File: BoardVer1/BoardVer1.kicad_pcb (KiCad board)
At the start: 2 copper layers, 80 parts, among them J1 Vin, J2 Motor conn, J3 FTDI_basic, J4 LED strip, J5 Swiss Sonic cable, J6 CycleStartBtn, J7 MicroSwitches, J8 Estop, J9 SonicGND, SW1 SW_Push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

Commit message: First layout complete
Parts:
- removed C1: 100uF, Capacitor_SMD:C_0805_2012Metric_Pad1.15x1.40mm_HandSolder
- removed C12, C13: 15p, Capacitor_SMD:C_0805_2012Metric_Pad1.15x1.40mm_HandSolder
- removed C8, C9: 100n, Capacitor_SMD:C_0805_2012Metric_Pad1.15x1.40mm_HandSolder
- removed D3: D_Schottky, Diode_SMD:D_SMB_Handsoldering
- removed J3: FTDI_basic, Connector_PinHeader_2.54mm:PinHeader_1x06_P2.54mm_Vertical
- removed L1: 47uH, Inductor_SMD:L_Neosid_SM-NE127_HandSoldering
- removed R2: 1K, Resistor_SMD:R_0805_2012Metric_Pad1.15x1.40mm_HandSolder
- removed R3: 3K, Resistor_SMD:R_0805_2012Metric_Pad1.15x1.40mm_HandSolder
- removed R4: 10K, Resistor_SMD:R_0805_2012Metric_Pad1.15x1.40mm_HandSolder
- removed SW1: SW_Push, Button_Switch_SMD:SW_SPST_B3S-1000
- removed U3: ATMEGA328PB-AU_Arduino, Package_QFP:TQFP-32_7x7mm_P0.8mm
- removed Y1: 16MHZ, Crystal:Crystal_HC49-4H_Vertical
- added A1: Arduino_Nano_v3.x, Module:Arduino_Nano, F.Cu at (174.8, 57.5)
- C15, C17, D1, R10, R11, R13, R17, R19, R22, R5, R6, R8: moved to B.Cu
- C2: value 100uF -> 10uF/50V; footprint Capacitor_SMD:C_0805_2012Metric_Pad1.15x1.40mm_HandSolder -> Capacitor_SMD:C_2010_5025Metric_Pad1.52x2.65mm_HandSolder
- C3: value 10n -> 22uF/16V; footprint Capacitor_SMD:C_0805_2012Metric_Pad1.15x1.40mm_HandSolder -> Capacitor_SMD:C_2010_5025Metric_Pad1.52x2.65mm_HandSolder
- F1: footprint Fuse:Fuse_1210_3225Metric_Pad1.42x2.65mm_HandSolder -> Fuse:Fuse_2010_5025Metric_Pad1.52x2.65mm_HandSolder; moved to B.Cu
- F2: footprint Fuse:Fuse_1210_3225Metric_Pad1.42x2.65mm_HandSolder -> Fuse:Fuse_2010_5025Metric_Pad1.52x2.65mm_HandSolder
- J1: footprint TerminalBlock_4Ucon:TerminalBlock_4Ucon_1x02_P3.50mm_Horizontal -> TerminalBlock:TerminalBlock_bornier-2_P5.08mm
- U2: value LM2675M-ADJ -> V7805-1000; footprint Package_SO:SOIC-8_3.9x4.9mm_P1.27mm -> digikey-footprints:3-SIP_Module_V7805-1000
- moved R11 329.8 mm to (127.2, 55.1)
- moved C14 328.6 mm to (118.1, 63.8), turned to 270 degrees
- moved R1 281.7 mm to (115.6, 70.1), turned to 270 degrees
- moved C10 275.8 mm to (111.0, 66.0), turned to 180 degrees
- moved R19 273.8 mm to (136.4, 129.3), turned to 90 degrees
- moved C15 256.3 mm to (133.9, 85.3)
- moved C17 248.7 mm to (136.9, 76.7), turned to 90 degrees
- moved R18 235.8 mm to (140.5, 124.0), turned to 270 degrees
- moved R21 235.8 mm to (153.2, 123.2)
- moved R22 232.7 mm to (156.2, 106.4)
- moved C2 225.5 mm to (161.5, 105.9), turned to 90 degrees
- moved C3 221.0 mm to (167.1, 106.2), turned to 90 degrees
- moved R10 220.2 mm to (160.0, 47.8), turned to 270 degrees
- moved R5 212.5 mm to (185.2, 62.5), turned to 180 degrees
- moved R9 208.7 mm to (170.9, 107.4), turned to 90 degrees
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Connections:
- C3 pad 1: Net-(C3-Pad1) -> VCC
- C3 pad 2: Net-(C3-Pad2) -> GND
- D5 pad 1: VCC -> GND
- U2 pad 1: Net-(C3-Pad2) -> +24V
- U2 pad 2: Net-(U2-Pad2) -> GND
- U2 pad 3: Net-(U2-Pad3) -> VCC
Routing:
- net VCC: track 115.2 -> 339.4 mm, vias 2 -> 5
- net +24V: track 3.72 -> 174.5 mm, vias 0 -> 2
- net SDA: track 0.00 -> 124.2 mm, vias 0 -> 1
- net SCL: track 0.00 -> 112.3 mm, vias 0 -> 1
- net CycleStart: track 0.00 -> 94.5 mm, vias 0 -> 1
- net Relay_act: track 0.00 -> 82.8 mm, vias 0 -> 1
- net PixelStrip: track 6.25 -> 79.6 mm, vias 1 -> 0
- net WindowShut: track 0.00 -> 65.1 mm, vias 0 -> 1
- net SCK: track 13.3 -> 60.4 mm, vias 0 -> 2
- net Net-(J5-Pad1): track 0.00 -> 40.3 mm, vias 0 -> 2
- net Sonic24V: track 0.00 -> 38.2 mm
- net Net-(JP2-Pad3): track 0.00 -> 37.0 mm
- net BTN1: track 0.00 -> 36.3 mm, vias 0 -> 2
- net Net-(RV1-Pad2): track 0.00 -> 33.6 mm, vias 0 -> 2
- net Net-(J5-Pad2): track 0.00 -> 33.2 mm, vias 0 -> 2
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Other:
- board outline added: 114.6 x 96.5 mm
- net class Default: clearance 0.23 -> 0.25; trace_width 0.35 -> 0.4
- rule trace_clearance: 0.23 -> 0.25

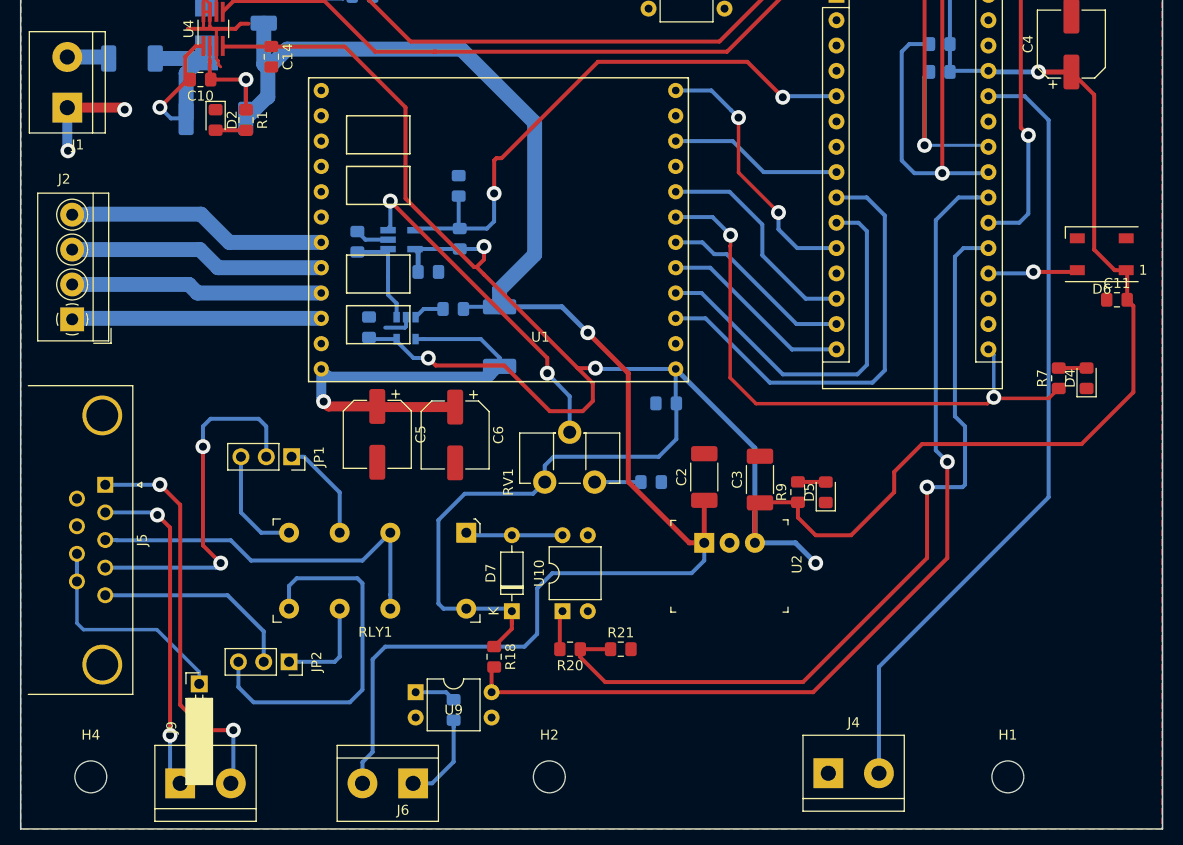
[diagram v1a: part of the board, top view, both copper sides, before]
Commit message: Less vias
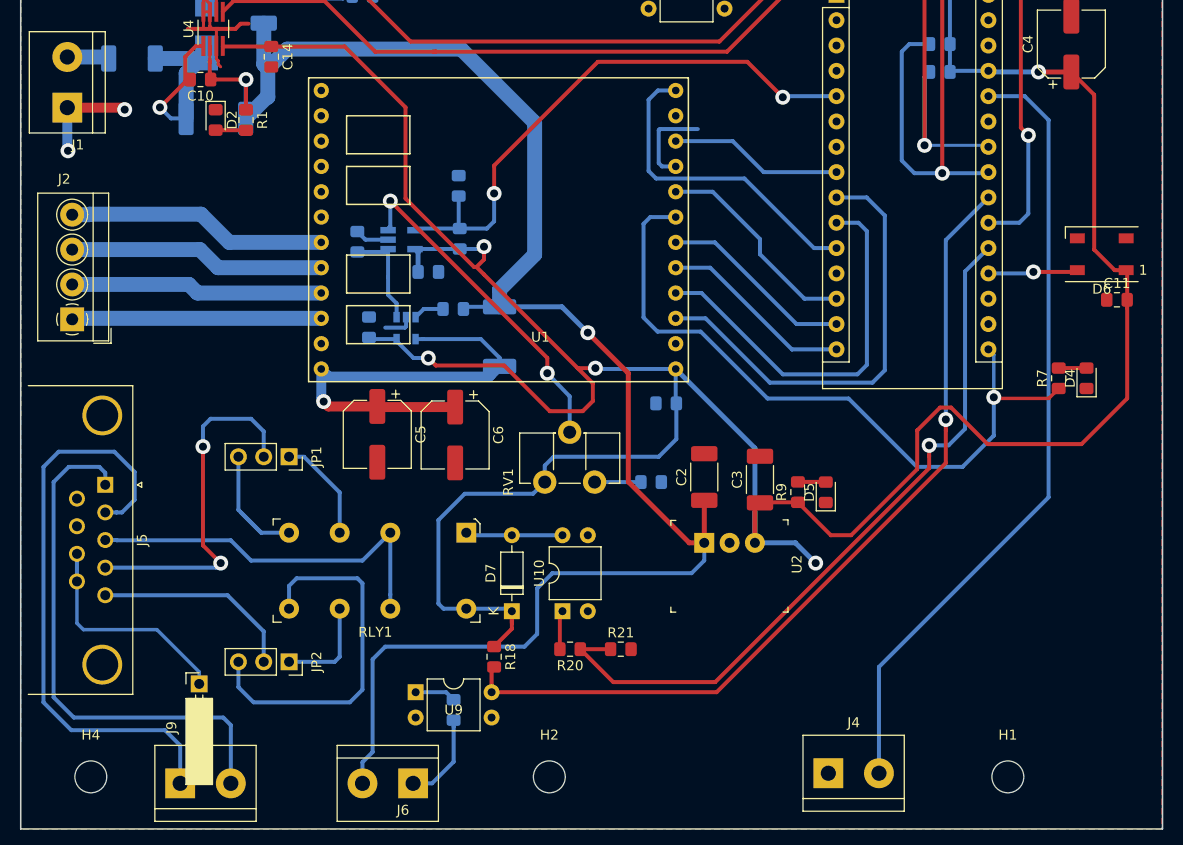
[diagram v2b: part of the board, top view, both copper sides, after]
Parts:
- moved JP1 0.25 mm to (119.9, 103.9)
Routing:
- net Net-(J5-Pad2): track 33.2 -> 61.3 mm, vias 2 -> 0
- net Net-(J5-Pad1): track 40.3 -> 54.0 mm, vias 2 -> 0
- net SCK: track 60.4 -> 71.4 mm, vias 2 -> 1
- net GND: track 37.3 -> 46.4 mm
- net Relay_act: track 82.8 -> 74.0 mm
- net CycleStart: track 94.5 -> 86.1 mm
- net StallGuard: track 26.9 -> 32.3 mm, vias 2 -> 0
- net Net-(JP1-Pad3): track 11.3 -> 14.2 mm
- net VCC: track 339.4 -> 342.1 mm
- net CSN: track 22.4 -> 21.5 mm
- net BTN1: track 36.3 -> 35.7 mm
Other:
- net class Default: via_drill 0.8 -> 1

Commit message: Better layout
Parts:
- removed J6: CycleStartBtn, TerminalBlock:TerminalBlock_bornier-2_P5.08mm
- removed J7: MicroSwitches, TerminalBlock:TerminalBlock_bornier-6_P5.08mm
- removed R21: 10K, Resistor_SMD:R_0805_2012Metric_Pad1.15x1.40mm_HandSolder
- removed RLY1: G5V-2-DC12, digikey-footprints:Relay_THT_G5V-2
- added R2: 1K-2K, Resistor_SMD:R_0805_2012Metric_Pad1.15x1.40mm_HandSolder, F.Cu at (146.7, 123.4)
- added R3: 10K, Resistor_SMD:R_0805_2012Metric_Pad1.15x1.40mm_HandSolder, B.Cu at (175.6, 122.7)
- added R4: G6A-274P, Libs:OMRON_G6A-274P-ST, F.Cu at (127.6, 119.6)
- added U3: PC817, Package_DIP:DIP-4_W7.62mm, F.Cu at (168.3, 126.2)
- J2: value Motor conn -> Screw_Terminal_01x12; footprint TerminalBlock_4Ucon:TerminalBlock_4Ucon_1x04_P3.50mm_Horizontal -> TerminalBlock_Phoenix:TerminalBlock_Phoenix_PT-1,5-12-3.5-H_1x12_P3.50mm_Horizontal
- J9: footprint Connector_PinSocket_2.54mm:PinSocket_1x01_P2.54mm_Horizontal -> Connector_PinHeader_2.54mm:PinHeader_1x01_P2.54mm_Vertical
- R11, R13, R19: moved to F.Cu
- R18, R20: moved to B.Cu
- moved J4 87.0 mm to (202.9, 53.6), turned to 90 degrees
- moved J2 33.4 mm to (99.1, 56.7), turned to 270 degrees
- moved J1 32.6 mm to (123.6, 49.1), turned to 180 degrees
- moved J9 20.1 mm to (95.2, 139.3)
- moved R18 19.5 mm to (159.9, 121.9)
- moved U9 19.3 mm to (151.9, 126.2)
- moved F2 18.1 mm to (112.6, 75.6), turned to 180 degrees
- moved R11 18.1 mm to (145.3, 56.1)
- moved R13 17.9 mm to (145.2, 58.9)
- moved D7 17.1 mm to (127.8, 110.2), turned to 180 degrees
- moved F1 15.7 mm to (110.6, 49.7), turned to 0 degrees
- moved U10 13.3 mm to (134.2, 117.1)
- moved JP1 12.1 mm to (111.1, 112.3), turned to 0 degrees
- moved R19 10.8 mm to (146.7, 126.1), turned to 0 degrees
- moved R20 9.37 mm to (141.0, 117.1), turned to 0 degrees
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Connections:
- A1 pad 25: Net-(A1-Pad25) -> PistonTop
- F2 pad 1: Net-(F2-Pad1) -> +24V
- F2 pad 2: +24V -> Net-(F2-Pad2)
- J2 pad 1: Net-(J2-Pad1) -> Net-(F2-Pad2)
- J2 pad 2: Net-(J2-Pad2) -> Net-(F2-Pad2)
- J2 pad 3: Net-(J2-Pad3) -> Net-(F2-Pad2)
- J2 pad 4: Net-(J2-Pad4) -> Net-(F2-Pad2)
- R11 pad 1: Net-(J7-Pad3) -> DoorOpenBTN
- R13 pad 1: Net-(J7-Pad1) -> WindowShutBTN
- R19 pad 1: Net-(J6-Pad1) -> CycleStartBtn
- R20 pad 1: Relay_act -> Net-(R20-Pad1)
- R20 pad 2: Net-(R20-Pad2) -> GND
- U1 pad 19: Net-(J2-Pad4) -> B2
- U1 pad 20: Net-(J2-Pad3) -> B1
- U1 pad 21: Net-(J2-Pad2) -> A2
- U1 pad 22: Net-(J2-Pad1) -> A1
- U10 pad 1: Net-(R20-Pad2) -> Relay_act
- U10 pad 2: GND -> Net-(R20-Pad1)
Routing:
- net PistonTopBTN: track 0.00 -> 87.0 mm, vias 0 -> 1
- net CycleStartBtn: track 0.00 -> 86.8 mm, vias 0 -> 1
- net PistonTop: track 0.00 -> 74.5 mm
- net WindowShutBTN: track 0.00 -> 70.0 mm, vias 0 -> 1
- net DoorOpenBTN: track 0.00 -> 67.3 mm, vias 0 -> 1
- net PixelStrip: track 79.6 -> 33.5 mm
- net +24V: track 174.5 -> 132.0 mm
- net Net-(F2-Pad1): track 31.3 -> 0.00 mm
- net Net-(F2-Pad2): track 0.00 -> 27.1 mm
- net A1: track 0.00 -> 26.2 mm
- net Net-(J2-Pad4): track 26.2 -> 0.00 mm
- net Net-(JP1-Pad1): track 10.4 -> 36.5 mm
- net A2: track 0.00 -> 25.8 mm
- net Net-(J2-Pad3): track 25.7 -> 0.00 mm
- net B1: track 0.00 -> 25.4 mm
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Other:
- net class Default: clearance 0.25 -> 0.3
- rule trace_clearance: 0.25 -> 0.3

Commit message: BOM and polish
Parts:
- F1, F2: footprint Fuse:Fuse_2010_5025Metric_Pad1.52x2.65mm_HandSolder -> Libs:LittleFuse_110F_24V
- moved F2 1.28 mm to (113.9, 75.7)
- moved F1 0.72 mm to (109.9, 49.5)
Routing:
- net SCL: track 112.3 -> 147.4 mm
- net SonicGND: track 2.77 -> 23.0 mm
- net +24V: track 132.0 -> 133.9 mm
- net Net-(C10-Pad2): track 36.0 -> 37.7 mm
- net WindowShut: track 64.8 -> 65.3 mm

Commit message: grbr
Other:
- net class Default: via_dia 1.5 -> 2.1; via_drill 1 -> 1.2
